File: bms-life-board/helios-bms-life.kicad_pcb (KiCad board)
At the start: 4 copper layers, 34 x 19 mm, 66 parts, among them J1 Debug, J2 Output, J3 Outboard, J4 Battery, Q1 NMOS, Q2 SSM3J332R, U1 TPSM861253, U2 STM32L011F4Ux, U3 TPS22811, U4 TPS563207s, U5 BQ25306, U6 THVD1400D

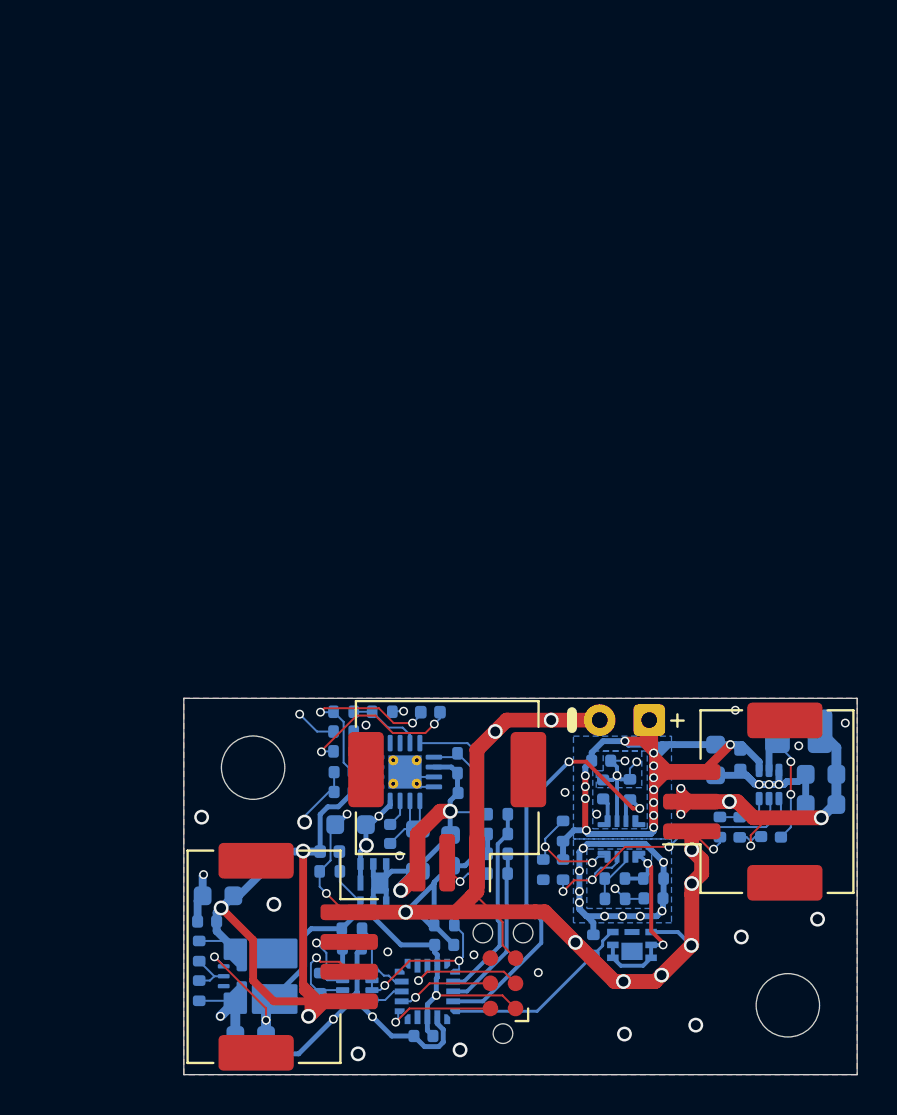
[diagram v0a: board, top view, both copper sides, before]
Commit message: post DR LiFe board partially done, need to clean up the BoM on digikey BADDD
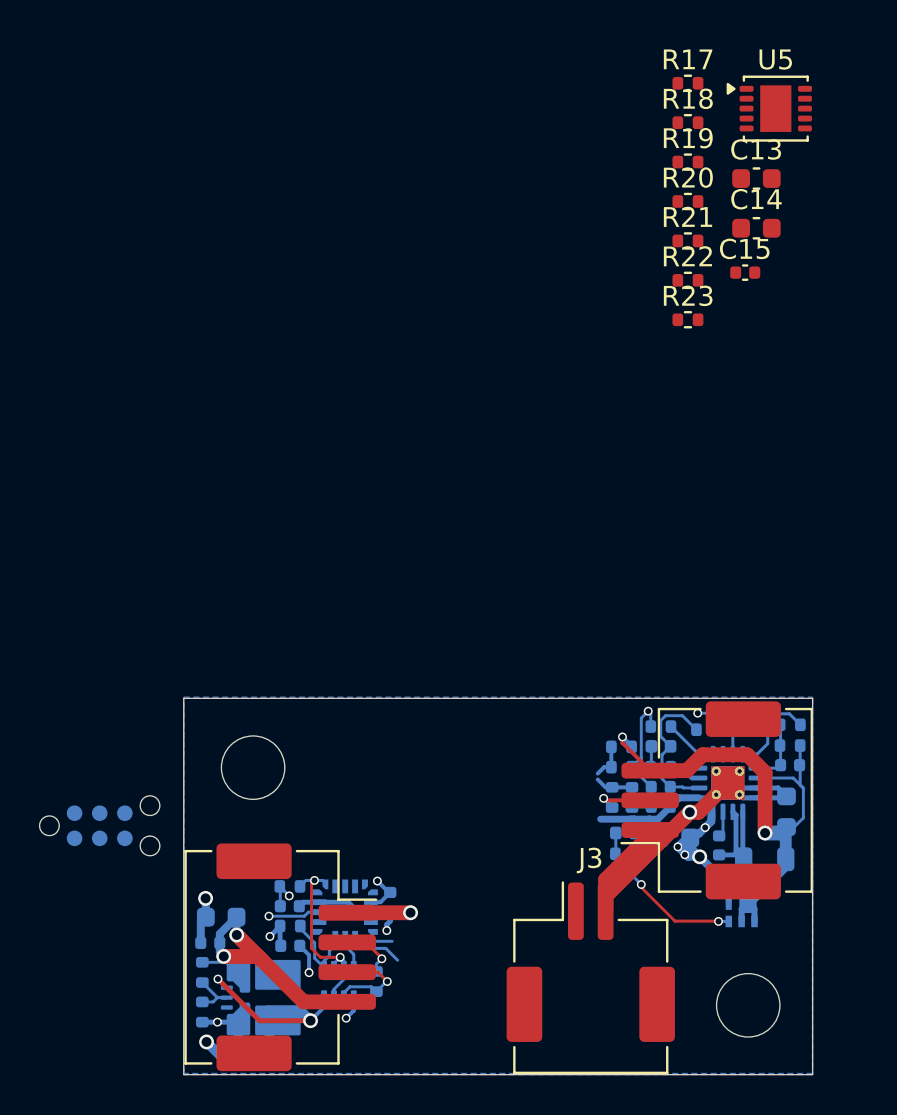
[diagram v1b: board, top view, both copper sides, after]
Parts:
- removed the C10 at (109.3, 73.6)
- removed the C11 at (106.0, 71.6)
- removed the C12 at (110.6, 73.6)
- removed C16: 22p, Capacitor_SMD:C_0402_1005Metric
- removed C17, C22: 10u, Capacitor_SMD:C_0603_1608Metric
- removed C18: 47n, Capacitor_SMD:C_0402_1005Metric
- removed C19, C21: 22u, Capacitor_SMD:C_0603_1608Metric
- removed C20: 470p, Capacitor_SMD:C_0402_1005Metric
- removed the C3 at (106.2, 80.6)
- removed the J2 at (110.7, 75.7)
- removed L2: 2.2uH, Inductor_SMD:L_0805_2012Metric
- removed Q2: SSM3J332R, Helios-BMS:SOT-1220_UDFN6B_TOS-L
- removed the R1 at (103.2, 83.0)
- removed the R10 at (101.7, 77.2)
- removed the R11 at (100.7, 79.2)
- removed the R12 at (101.7, 79.2)
- removed the R13 at (90.6, 72.2)
- removed the R14 at (90.6, 73.2)
- removed the R15 at (110.6, 77.0)
- removed the R16 at (109.6, 77.0)
- removed the U3 at (104.6, 77.6)
- removed the U4 at (112.0, 74.8)
- added C4: 10u, Capacitor_SMD:C_0603_1608Metric, B.Cu at (107.3, 77.5)
- added C6: 47n, Capacitor_SMD:C_0402_1005Metric, B.Cu at (109.5, 77.9)
- added C7: 2.2u, Capacitor_SMD:C_0402_1005Metric, B.Cu at (106.6, 75.0)
- added C8: 10u, Capacitor_SMD:C_0603_1608Metric, B.Cu at (112.9, 76.2)
- added J3: Output, Connector_JST:JST_ZE_SM02B-ZESS-TB_1x02-1MP_P1.50mm_Horizontal, F.Cu at (103.0, 83.8)
- added R22: 100k, Resistor_SMD:R_0402_1005Metric, F.Cu at (108.0, 49.4)
- added R23: 2.49k, Resistor_SMD:R_0402_1005Metric, F.Cu at (108.0, 51.4)
- added R3: 10k, Resistor_SMD:R_0402_1005Metric, B.Cu at (104.8, 78.3)
- added R7: 200k, Resistor_SMD:R_0402_1005Metric, B.Cu at (113.1, 71.8)
- added R8: 10k, Resistor_SMD:R_0402_1005Metric, B.Cu at (108.9, 72.1)
- added U2: BQ25306, Package_DFN_QFN:WQFN-16-1EP_3x3mm_P0.5mm_EP1.68x1.68mm_ThermalVias, B.Cu at (110.0, 74.8)
- C13, C14: value 2.2u -> 10u; footprint Capacitor_SMD:C_0402_1005Metric -> Capacitor_SMD:C_0603_1608Metric; moved to F.Cu
- C15: value 0.1u -> 10n; moved to F.Cu
- C5: value 1.5n -> 2.2u
- C9: value 1u -> 470p
- D1: value Status -> TBD; footprint LED_SMD:LED_0402_1005Metric -> Diode_SMD:D_0402_1005Metric
- D2: value TBD -> Status; footprint Diode_SMD:D_0402_1005Metric -> LED_SMD:LED_0402_1005Metric
- J2: renamed from J1; moved to B.Cu
- L1: value 3.3uH -> 2.2uH; footprint Inductor_SMD:L_1008_2520Metric -> Inductor_SMD:L_0805_2012Metric
- Q1: value NMOS -> SSM3J332R
- R17, R18: value 10k -> 100k; moved to F.Cu
- R19: value 1.1M -> 100k; moved to F.Cu
- R20: value 200k -> 267k; moved to F.Cu
- R21: value 100k -> 10k; moved to F.Cu
- R4: value 430k -> 300
- R5: value 100k -> 1.1M
- R6: value 51k -> 160k
- R9: value 1k -> 10k
- U5: value BQ25306 -> SIP32434; footprint Package_DFN_QFN:WQFN-16-1EP_3x3mm_P0.5mm_EP1.68x1.68mm_ThermalVias -> Package_DFN_QFN:Maxim_TDFN-10-1EP_3x3mm_P0.5mm_EP1.58x2.35mm; moved to F.Cu
- moved U5 38.4 mm to (112.4, 40.7)
- moved C13 37.3 mm to (111.4, 44.3), turned to 0 degrees
- moved R21 36.6 mm to (108.0, 47.4), turned to 0 degrees
- moved R17 36.2 mm to (108.0, 39.4), turned to 0 degrees
- moved C14 34.5 mm to (111.4, 46.8), turned to 0 degrees
- moved R18 33.5 mm to (108.0, 41.4)
- moved R19 32.8 mm to (108.0, 43.4)
- moved R20 30.0 mm to (108.0, 45.4)
- moved C15 28.1 mm to (110.8, 49.0), turned to 0 degrees
- moved J2 21.9 mm to (78.3, 76.9), turned to 0 degrees
- moved D2 17.5 mm to (106.6, 72.9), turned to 0 degrees
- moved J4 12.8 mm to (108.6, 75.7), turned to 90 degrees
- moved D1 11.6 mm to (104.8, 77.3), turned to 0 degrees
- moved R5 11.1 mm to (113.1, 72.9)
- moved C9 9.54 mm to (113.1, 73.9), turned to 180 degrees
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- renumbered C6 to C10, C4 to C11, C23 to C12, C8 to C3, J3 to J1, R2 to R1, R22 to R10, R24 to R11, R23 to R12, R7 to R13, R25 to R14, R8 to R15, R26 to R16, R3 to R2, U2 to U3, U6 to U4
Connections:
- C13 pad 1: +12V -> VSYS
- C14 pad 1: /REGN -> +VSW
- C15 pad 1: Net-(U4-SW) -> Net-(U5-SS)
- C15 pad 2: Net-(U4-BST) -> GND
- C5 pad 1: Net-(U3-DV/DT) -> +12V
- C9 pad 1: +VSW -> +BATT
- C9 pad 2: GND -> Net-(U2-FB)
- D1 pad 2: /REGN -> +12V
- D2 pad 2: +12V -> /REGN
- L1 pad 1: Net-(U4-SW) -> Net-(C6-Pad1)
- L1 pad 2: +3V7 -> +BATT
- Q1 pad 1: /EN/UVLO -> +BATT
- Q1 pad 2: /EN/UVLO -> +BATT
- Q1 pad 3: /GATE -> Net-(D1-K)
- Q1 pad 4: GND -> VSYS
- Q1 pad 5: /EN/UVLO -> +BATT
- Q1 pad 6: /EN/UVLO -> +BATT
- Q1 pad 7: unconnected-(Q1-Pad7) -> +BATT
- Q1 pad 8: unconnected-(Q1-Pad8) -> VSYS
- R17 pad 1: Net-(U5-TS) -> Net-(Q2-S)
- R17 pad 2: /REGN -> Net-(Q2-G)
- R18 pad 1: Net-(U5-TS) -> /GATE
- R19 pad 1: +BATT -> Net-(Q2-D)
- R19 pad 2: Net-(U5-FB) -> GND
- R20 pad 1: Net-(U5-FB) -> Net-(U5-OVP)
- R20 pad 2: Net-(U5-FB_GND) -> VSYS
- R21 pad 1: Net-(D2-K) -> /SW_PG
- R21 pad 2: GND -> +3.3V
- R4 pad 1: VSYS -> Net-(D2-K)
- R4 pad 2: /EN/UVLO -> Net-(U2-STAT)
- R5 pad 1: /EN/UVLO -> +BATT
- R5 pad 2: /~{EN}/OVLO -> Net-(U2-FB)
- R6 pad 1: /~{EN}/OVLO -> Net-(U2-ICHG)
- R9 pad 1: /IMON -> Net-(U2-TS)
- U3 pad 14: unconnected-(U2-PA9-Pad14) -> /SW_PG
- U5 pad 1: +12V -> VSYS
- U5 pad 10: +BATT -> +VSW
- U5 pad 2: /REGN -> VSYS
- U5 pad 3: Net-(U5-STAT) -> Net-(U5-SS)
- U5 pad 4: Net-(U5-ICHG) -> /EN/UVLO
- U5 pad 5: unconnected-(U5-POL-Pad5) -> /IMON
- U5 pad 6: unconnected-(U5-~{EN}-Pad6) -> GND
- U5 pad 7: Net-(U5-TS) -> Net-(U5-OVP)
- U5 pad 8: Net-(U5-FB_GND) -> /SW_PG
- U5 pad 9: Net-(U5-FB) -> +VSW
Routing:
- net GND: track 118.1 -> 55.3 mm, vias 44 -> 11
- net +VSW: track 56.3 -> 0.00 mm, vias 13 -> 0
- net /IMON: track 22.4 -> 0.00 mm, vias 2 -> 0
- net +3V7: track 21.2 -> 0.00 mm, vias 5 -> 0
- net +12V: track 40.0 -> 22.0 mm, vias 3 -> 2
- net /SW_PG: track 15.9 -> 0.00 mm, vias 3 -> 0
- net VSYS: track 21.7 -> 9.48 mm, vias 11 -> 4
- net /EN/UVLO: track 11.2 -> 0.00 mm, vias 2 -> 0
- net /GATE: track 9.69 -> 0.00 mm
- net /PACK_ADC: track 10.00 -> 1.85 mm
- net Net-(U4-SW): track 7.99 -> 0.00 mm, vias 2 -> 0
- net +BATT: track 22.4 -> 30.1 mm
- net /CENTER_TAP_ADC: track 8.50 -> 1.91 mm
- net Net-(C6-Pad1): track 0.00 -> 6.36 mm
- net Net-(U3-PGTH): track 6.09 -> 0.00 mm, vias 2 -> 0
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- removed copper zone on In2.Cu, net +12V
- removed copper zone on In2.Cu, net +3V7
- removed copper zone on B.Cu, net +VSW
- removed copper zone on In2.Cu, net +VSW
- removed copper zone on B.Cu, net VSYS
- removed copper zone on In2.Cu, net VSYS
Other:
- board size 34 x 19 mm -> 31.8 x 19 mm

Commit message: LiFe board done
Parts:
- added Q2: Q_Dual_NMOS_PMOS_S1G1D2S2G2D1, Package_TO_SOT_SMD:SOT-666, B.Cu at (100.1, 77.9)
- added Q3: PMOS, Package_TO_SOT_SMD:SOT-723, B.Cu at (100.0, 80.0)
- C13, C14, C15, R17, R18, R19, R20, R21, R22, R23, U5: moved to B.Cu
- J2: moved to F.Cu
- moved U5 44.9 mm to (102.1, 84.5), turned to 180 degrees
- moved C13 40.8 mm to (107.1, 84.8), turned to -90 degrees
- moved R21 39.9 mm to (96.7, 85.7), turned to -90 degrees
- moved C14 39.8 mm to (98.4, 84.4), turned to -90 degrees
- moved R17 39.8 mm to (98.0, 78.0), turned to 90 degrees
- moved C15 37.5 mm to (105.7, 86.1), turned to -90 degrees
- moved R20 36.9 mm to (103.4, 82.1)
- moved R18 36.8 mm to (103.1, 77.9), turned to 90 degrees
- moved R19 35.0 mm to (102.1, 77.9), turned to 90 degrees
- moved R23 34.9 mm to (104.7, 86.1), turned to 90 degrees
- moved R22 33.3 mm to (101.5, 82.1), turned to 180 degrees
- moved J2 16.8 mm to (94.8, 74.0), turned to 90 degrees
- moved R1 3.12 mm to (86.6, 84.2)
- moved R2 3.12 mm to (86.6, 86.2)
- moved U4 3.12 mm to (93.5, 84.7)
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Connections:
- J3 pad 1: +VSW -> GND
- J3 pad 2: GND -> +VSW
- R17 pad 1: Net-(Q2-S) -> +12V
- U3 pad 10: /GATE -> /IMON
- U3 pad 9: /IMON -> /GATE
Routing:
- net VSYS: track 9.48 -> 35.7 mm, vias 4 -> 8
- net +12V: track 22.0 -> 48.2 mm, vias 2 -> 7
- net +3.3V: track 31.4 -> 50.6 mm
- net GND: track 55.3 -> 73.9 mm, vias 11 -> 30
- net +VSW: track 0.00 -> 14.7 mm, vias 0 -> 2
- net /IMON: track 0.00 -> 14.1 mm, vias 0 -> 2
- net /PACK_ADC: track 1.85 -> 14.7 mm
- net /GATE: track 0.00 -> 12.8 mm
- net /SWCLK: track 2.77 -> 15.3 mm, vias 0 -> 1
- net /~{RESET}: track 2.63 -> 15.0 mm
- net /CENTER_TAP_ADC: track 1.91 -> 14.1 mm
- net /EN/UVLO: track 0.00 -> 11.3 mm, vias 0 -> 2
- net /SWDIO: track 1.37 -> 11.4 mm, vias 0 -> 1
- net /SW_PG: track 0.00 -> 8.99 mm
- net Net-(U5-OVP): track 0.00 -> 8.54 mm, vias 0 -> 2
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- added copper zone on In2.Cu, net GND
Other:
- board size 31.8 x 19 mm -> 28.6 x 19 mm
- board text added: "2S LiFe BMS Satellite Project Helios 2026"
- board text added: "<-Outside World"
- board text added: "Fueled by hate, powered by love."
- board text added: "Here be Volts->"
- board text added: "Kaboom->"
- board text added: "Nic DeBruin KV0R"
- board text added: "Why the long face?"
